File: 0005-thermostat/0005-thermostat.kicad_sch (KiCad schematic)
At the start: 19 parts, among them J1 NTC1, J3 12V, P1 22k, P2 22k

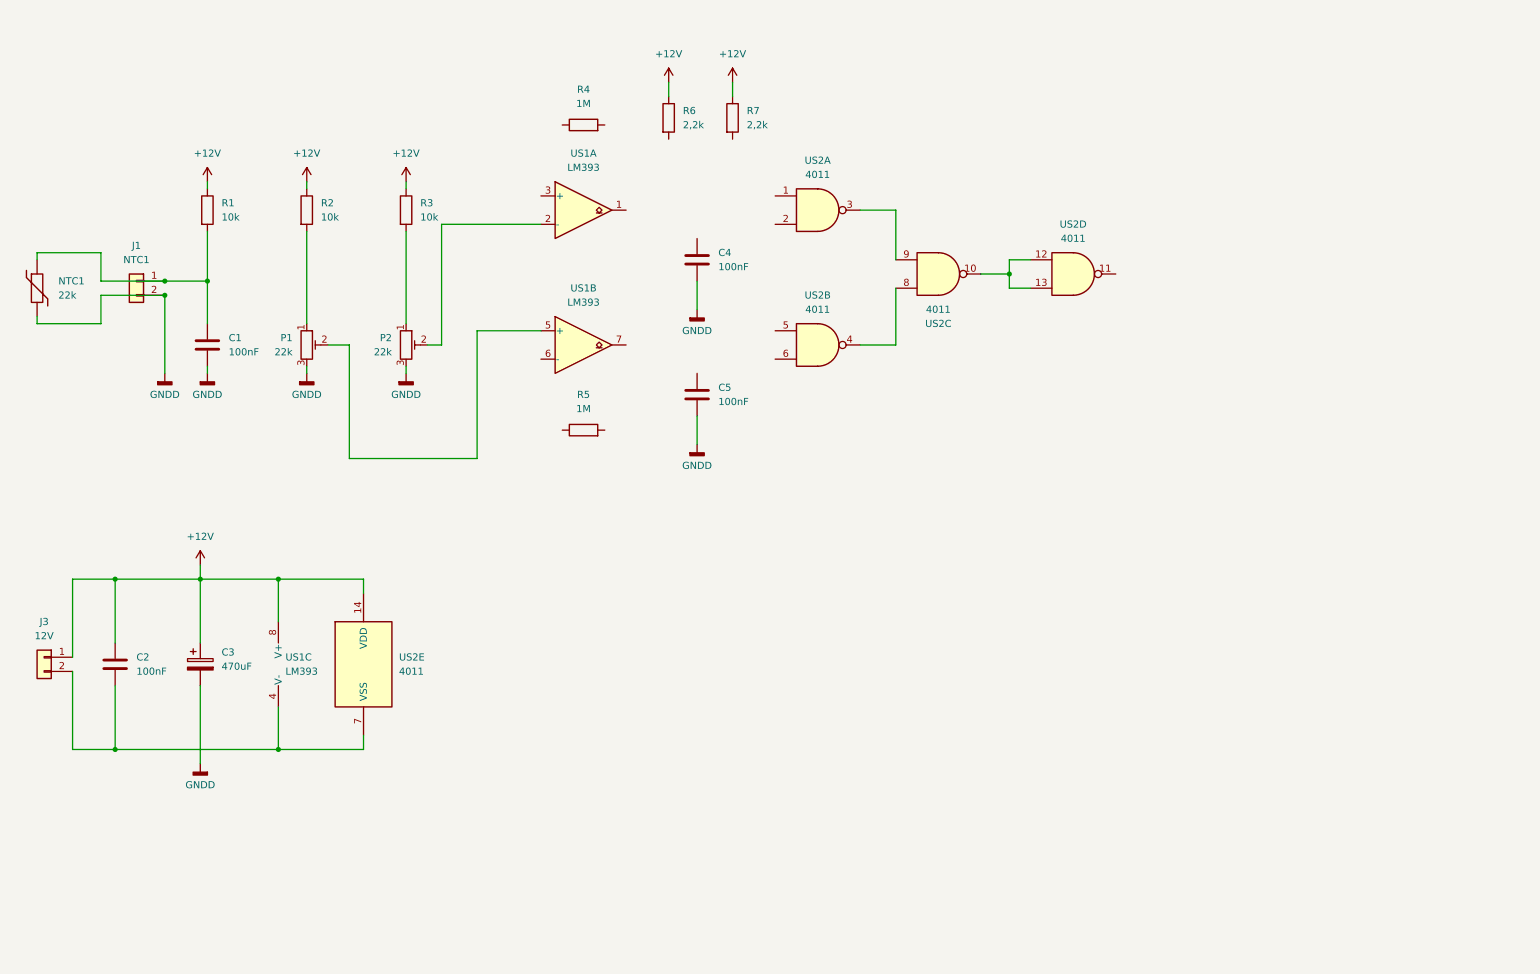
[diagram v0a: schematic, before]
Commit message: Add jumber for thermistor
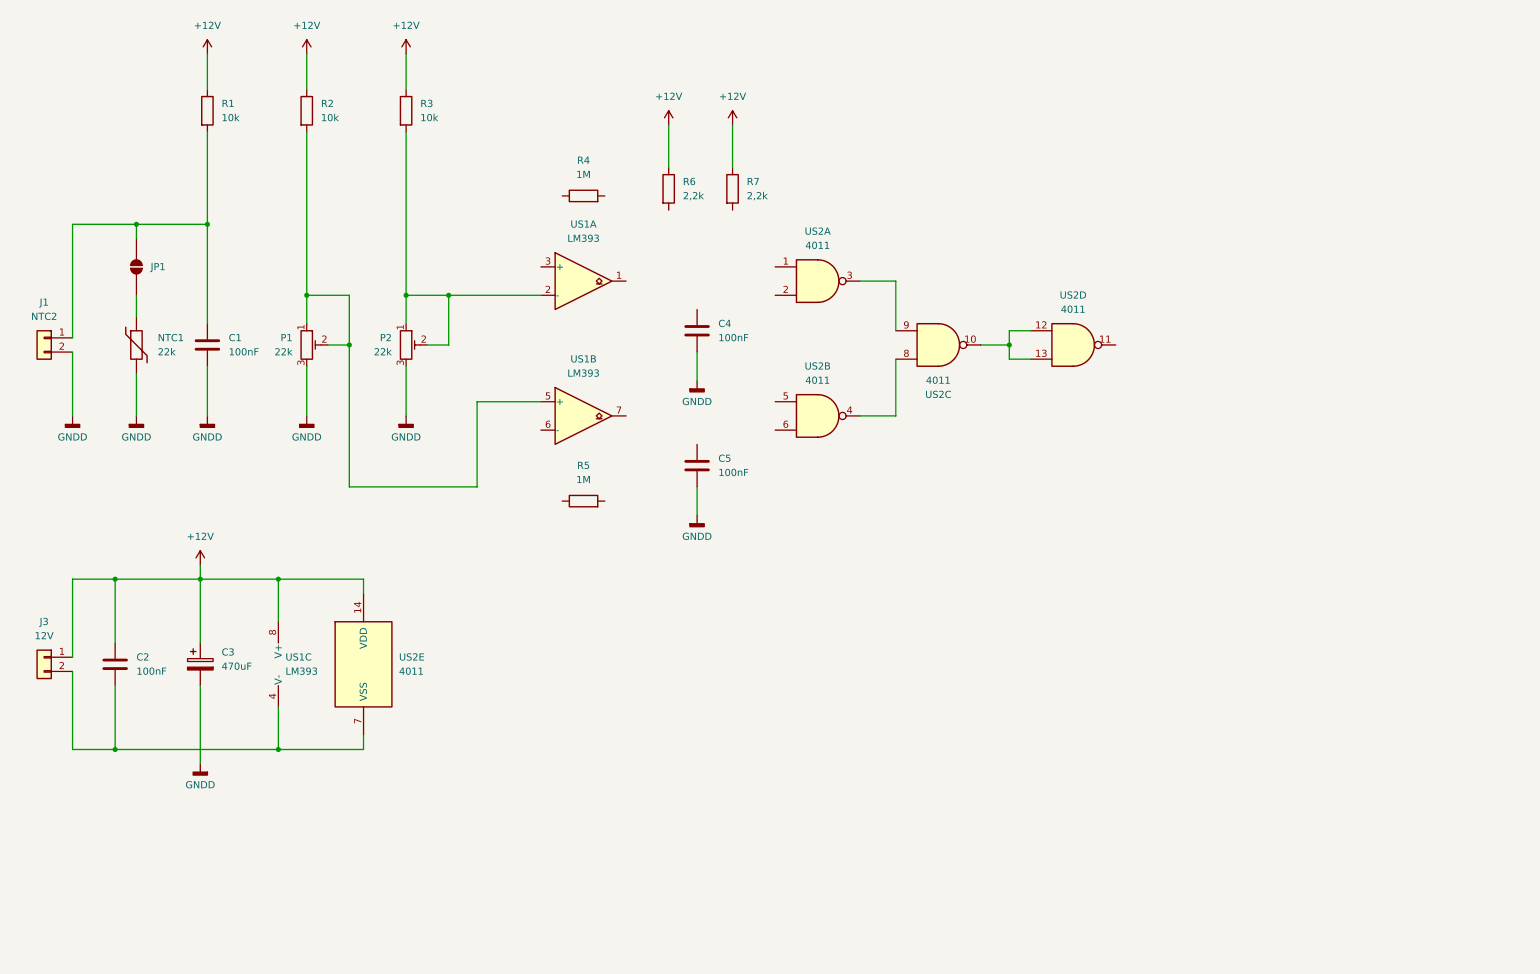
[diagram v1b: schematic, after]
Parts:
- added JP1: SolderJumper_2_Open, symbol Jumper:SolderJumper_2_Open
- J1: value NTC1 -> NTC2
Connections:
- net at P1.1, R2.2: now also P1.2, US1.5 (+)
- net at P2.1, R3.2: now also P2.2, US1.2 (-)
- net at C1.1, J1.1 (Pin_1), R1.2: now also JP1.2 (B); no longer NTC1.1
- new net: JP1.1 (A), NTC1.1
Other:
- moved on the sheet: C4, C5, J1, NTC1, R1, R2, R3, R4, R5, R6, R7, US1A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

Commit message: Schematic complete
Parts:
- added D1, D2, D3: 1N4148, Diode_THT:D_DO-35_SOD27_P7.62mm_Horizontal, symbol Diode:1N4148
- added J2: OUT, symbol Connector_Generic:Conn_01x04
- added J4: EXT_LED, symbol Connector_Generic:Conn_01x04
- added JP1, JP2, JP3, JP4, JP5, JP6: SolderJumper_2_Open, symbol Jumper:SolderJumper_2_Open
- added LED1: RED, symbol Device:LED
- added LED2: GREEN, symbol Device:LED
- added LED3: BLUE, symbol Device:LED
- added R10, R8, R9: 15k, symbol Device:R
- added R11, R12, R13, R14, R15, R16: 1k, symbol Device:R
- added T1, T2, T3: BC847B, Package_TO_SOT_SMD:SOT-23, symbol Transistor_BJT:BC847
- renumbered JP1 to JP4
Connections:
- net +12V: now also J3.+12 (Pin_1), D1.1 (K), D2.1 (K), D3.1 (K), J2.+12 (Pin_4), J4.+12 (Pin_4), JP1.2 (B), JP2.2 (B), JP3.2 (B), JP4.2 (B), JP5.2 (B), JP6.2 (B); no longer J3.1 (Pin_1)
- net GNDD: now also JP4.1 (A), T1.2 (E), T2.2 (E), T3.2 (E); no longer NTC1.2
- net at C4.1: now also R4.2, R7.2, US1.1, US2.1, US2.2, R10.1
- net at P1.1, P1.2, R2.2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: now also R5.1
- net at US2.5: now also C5.1, R5.2, R6.2, US1.7, US2.6, R8.1
- net at C2.2, US1.4 (V-), US2.7 (VSS): now also J3.GNDD (Pin_2); no longer J3.2 (Pin_2)
- net at US1.6 (-): now also C1.1, J1.1 (Pin_1), NTC1.1, R1.2, R4.1, US1.3 (+)
- net at US2.11: now also R9.1
- new net: R8.2, T1.1 (B)
- new net: D1.2 (A), J2.~{HI} (Pin_3), LED1.1 (K), R14.1, T1.3 (C)
- new net: D3.2 (A), J2.~{LO} (Pin_1), LED3.1 (K), R16.1, T3.3 (C)
- new net: D2.2 (A), J2.~{OK} (Pin_2), LED2.1 (K), R15.1, T2.3 (C)
- new net: JP2.1 (A), R12.1
- new net: LED3.2 (A), R13.2
- new net: JP3.1 (A), R13.1
- new net: R10.2, T3.1 (B)
- new net: LED2.2 (A), R12.2
- new net: J4.~{OK} (Pin_2), JP5.1 (A), R15.2
- new net: J4.~{HI} (Pin_3), JP4.1 (A), R14.2
- new net: J4.~{LO} (Pin_1), JP6.1 (A), R16.2
- new net: JP1.1 (A), R11.1
- new net: R9.2, T2.1 (B)
- new net: LED1.2 (A), R11.2
- new net: JP4.2 (B), NTC1.2
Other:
- moved on the sheet: C2, C3, C4, C5, J3, JP4, NTC1, R1, R2, R3, R6, R7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

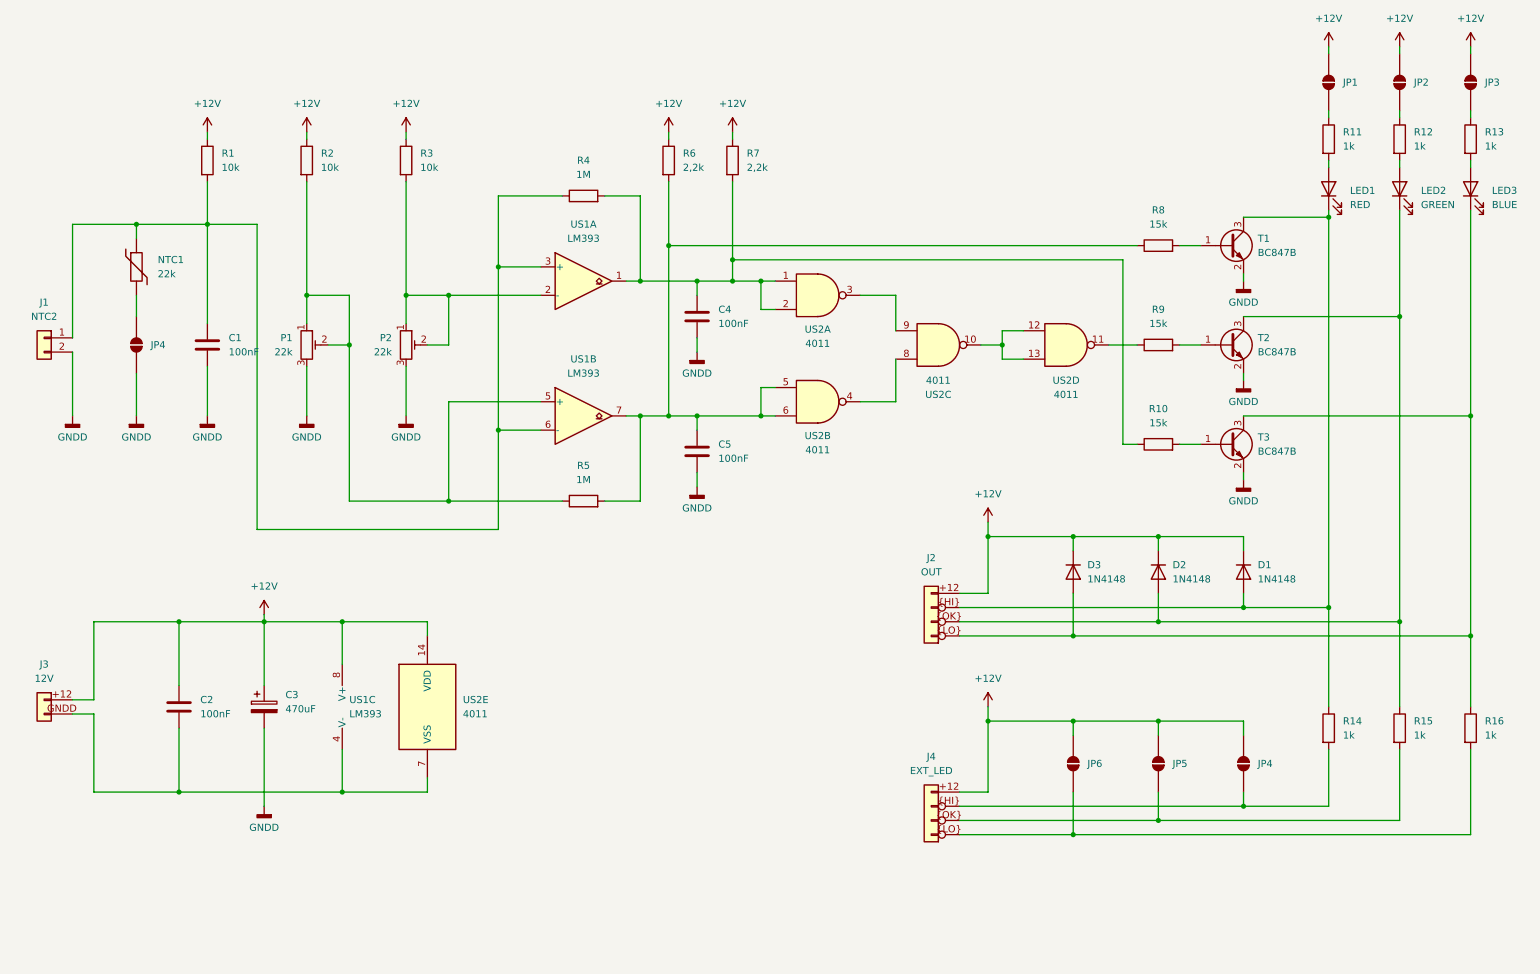
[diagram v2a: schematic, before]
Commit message: Schematic enhancement
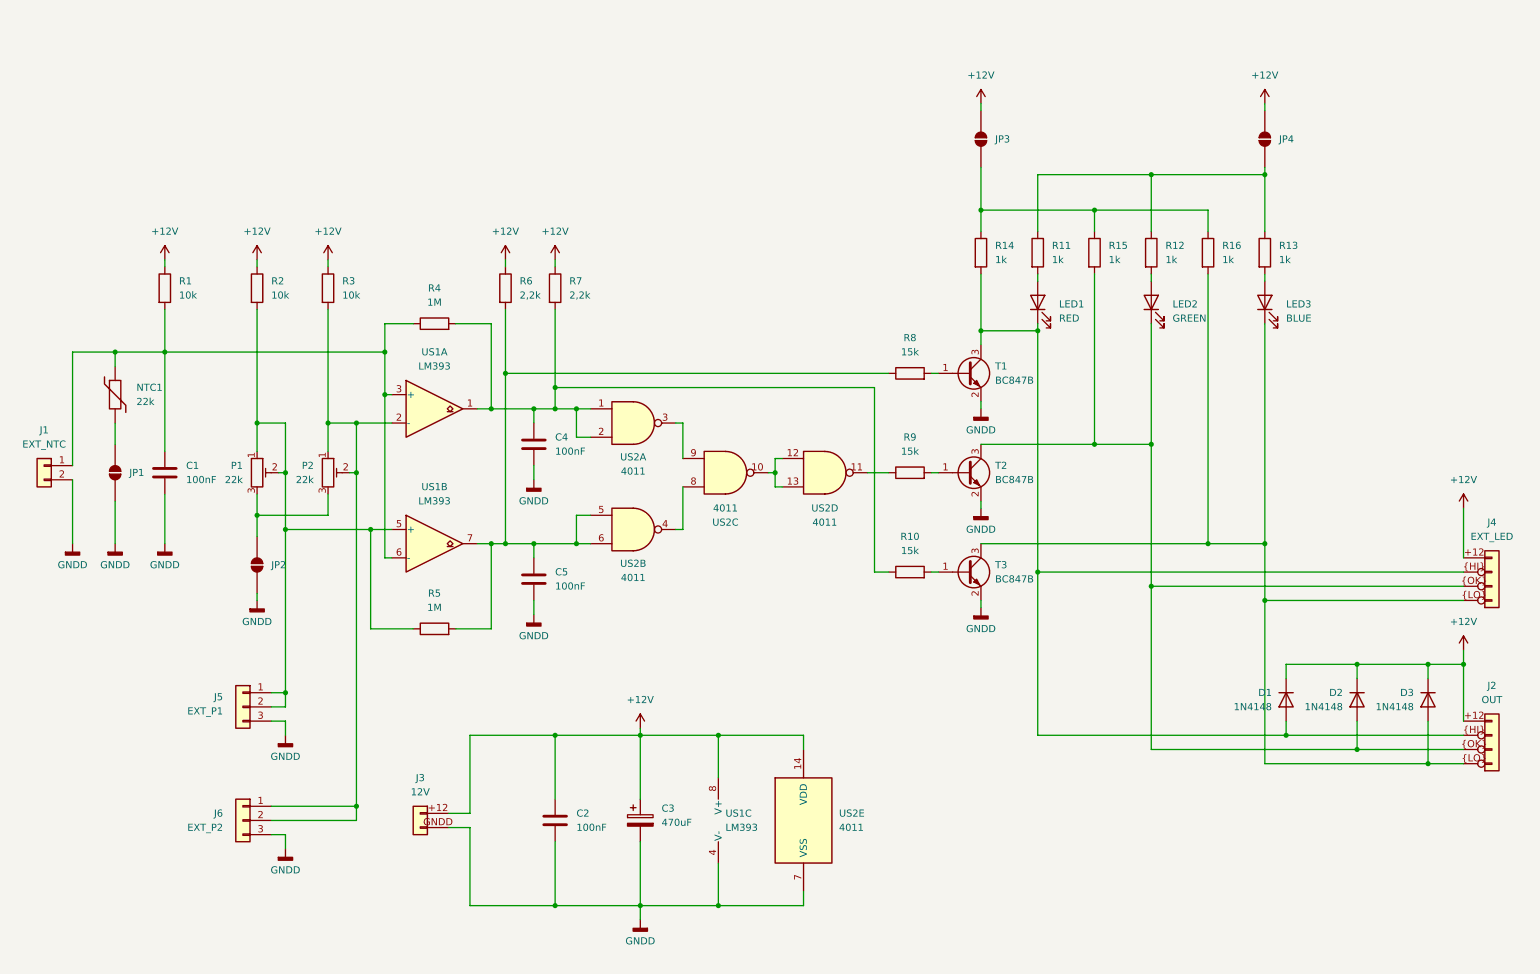
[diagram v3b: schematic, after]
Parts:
- removed JP4, JP5, JP6: SolderJumper_2_Open, symbol Jumper:SolderJumper_2_Open
- added J5: EXT_P1, symbol Connector_Generic:Conn_01x03
- added J6: EXT_P2, symbol Connector_Generic:Conn_01x03
- J1: value NTC2 -> EXT_NTC
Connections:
- net +12V: now also JP4.1 (A); no longer JP1.2 (B), JP2.2 (B)
- net GNDD: now also C2.2, J3.GNDD (Pin_2), JP1.1 (A), JP2.1 (A), US1.4 (V-), US2.7 (VSS), J5.3 (Pin_3), J6.3 (Pin_3); no longer JP4.1 (A), P1.3, P2.3
- net at P1.1, P1.2, R2.2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: now also J5.1 (Pin_1), J5.2 (Pin_2)
- net at D1.2 (A), J2.~{HI} (Pin_3), LED1.1 (K)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: now also J4.~{HI} (Pin_3), R14.2; no longer R14.1
- net at D3.2 (A), J2.~{LO} (Pin_1), LED3.1 (K)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: now also J4.~{LO} (Pin_1), R16.2; no longer R16.1
- net at D2.2 (A), J2.~{OK} (Pin_2), LED2.1 (K)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: now also J4.~{OK} (Pin_2), R15.2; no longer R15.1
- net at R12.1: now also JP4.2 (B), R11.1, R13.1; no longer JP2.1 (A)
- net at JP3.1 (A): now also R14.1, R15.1, R16.1; no longer R13.1
- net at P2.1, P2.2, R3.2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: now also J6.1 (Pin_1), J6.2 (Pin_2)
- net at NTC1.2: now also JP1.2 (B); no longer JP4.2 (B)
- new net: JP2.2 (B), P1.3, P2.3
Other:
- moved on the sheet: C1, C2, C3, C4, C5, D1, D2, D3, J1, J2, J3, J4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

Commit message: Update footprints
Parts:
- D1, D2, D3: footprint Diode_THT:D_DO-35_SOD27_P7.62mm_Horizontal -> Diode_SMD:D_SOD-323_HandSoldering
- R13: footprint (none) -> Resistor_SMD:R_0603_1608Metric_Pad0.98x0.95mm_HandSolder
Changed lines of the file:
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@@
 			)
 		)
-		(property "Footprint" ""
+		(property "Footprint" "Resistor_SMD:R_0603_1608Metric_Pad0.98x0.95mm_HandSolder"
 			(at 235.712 58.42 90)
 			(hide yes)
@@
 			)
 		)
-		(property "Footprint" "Diode_THT:D_DO-35_SOD27_P7.62mm_Horizontal"
+		(property "Footprint" "Diode_SMD:D_SOD-323_HandSoldering"
 			(at 254 138.43 0)
 			(hide yes)
@@
 			)
 		)
-		(property "Footprint" "Diode_THT:D_DO-35_SOD27_P7.62mm_Horizontal"
+		(property "Footprint" "Diode_SMD:D_SOD-323_HandSoldering"
 			(at 241.3 138.43 0)
 			(hide yes)
@@
 			)
 		)
-		(property "Footprint" "Diode_THT:D_DO-35_SOD27_P7.62mm_Horizontal"
+		(property "Footprint" "Diode_SMD:D_SOD-323_HandSoldering"
 			(at 266.7 138.43 0)
 			(hide yes)

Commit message: Enhance schematic and fix validation errors
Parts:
- J3: value 12V -> PWR
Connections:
- net +12V: now also J2.1 (Pin_1), J3.1 (Pin_1), J4.1 (Pin_1); no longer J2.+12 (Pin_4), J3.+12 (Pin_1), J4.+12 (Pin_4)
- net GNDD: now also J3.2 (Pin_2); no longer J3.GNDD (Pin_2)
- net at D1.2 (A), LED1.1 (K), R14.2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: now also J2.2 (Pin_2), J4.2 (Pin_2); no longer J2.~{HI} (Pin_3), J4.~{HI} (Pin_3)
- net at D3.2 (A), LED3.1 (K), R16.2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: now also J2.4 (Pin_4), J4.4 (Pin_4); no longer J2.~{LO} (Pin_1), J4.~{LO} (Pin_1)
- net at D2.2 (A), LED2.1 (K), R15.2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: now also J2.3 (Pin_3), J4.3 (Pin_3); no longer J2.~{OK} (Pin_2), J4.~{OK} (Pin_2)
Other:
- moved on the sheet: C1, C2, C3, C4, C5, D1, D2, D3, J1, J5, J6, JP1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

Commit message: Export schematic and place in README
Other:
- company: (none) -> ${GH_REPO}
- title: (none) -> Thermostat
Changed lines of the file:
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@@
 	(generator_version "10.0")
 	(paper "A4")
+	(title_block
+		(title "Thermostat")
+		(date "${CURRENT_DATE}")
+		(rev "${VERSION}")
+		(company "${GH_REPO}")
+	)
 	(junction
 		(at 113.03 110.49)
